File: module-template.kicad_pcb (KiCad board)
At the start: 2 copper layers, 0 parts

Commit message: Added PCB Essentials
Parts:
- added J1: 2X6-HEADERS, EC:M20-7810645, F.Cu at (111.7, 99.5)
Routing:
- net (no net): vias 0 -> 1
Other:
- board outline added: 95 x 25 mm
- board text added: "THIS SIDE DOWN"
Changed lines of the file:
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@@
   )
   (net 0 "")
+  (footprint "EC:M20-7810645" (layer "F.Cu")
+    (at 111.7011 99.5 90)
+    (descr "Harwin M20-7810645 Pass-Through Female Header")
+    (property "Sheetfile" "EC.kicad_sch")
+    (property "Sheetname" "")
+    (fp_text reference "J1" (at 0 0 90) (layer "F.SilkS") hide
+        (effects (font (size 1.27 1.27) (thickness 0.15)))
+    )
+    (fp_text value "2X6-HEADERS" (at 0 0 90) (layer "F.Fab") hide
+        (effects (font (size 1.27 1.27) (thickness 0.15)))
+    )
+    (pad "" np_thru_hole circle (at -6.35 -1.27 90) (size 1.02 1.02) (drill 1.02) (layers "F&B.Cu" "*.Mask"))
+    (pad "" np_thru_hole circle (at -6.35 1.27 90) (size 1.02 1.02) (drill 1.02) (layers "F&B.Cu" "*.Mask"))
+    (pad "" np_thru_hole circle (at -5.08 0 90) (size 1.8 1.8) (drill 1.8) (layers "F&B.Cu" "*.Mask"))
+    (pad "" np_thru_hole circle (at -3.81 -1.27 90) (size 1.02 1.02) (drill 1.02) (layers "F&B.Cu" "*.Mask"))
+    (pad "" np_thru_hole circle (at -3.81 1.27 90) (size 1.02 1.02) (drill 1.02) (layers "F&B.Cu" "*.Mask"))
+    (pad "" np_thru_hole circle (at -1.27 -1.27 90) (size 1.02 1.02) (drill 1.02) (layers "F&B.Cu" "*.Mask"))
+    (pad "" np_thru_hole circle (at -1.27 1.27 90) (size 1.02 1.02) (drill 1.02) (layers "F&B.Cu" "*.Mask"))
+    (pad "" np_thru_hole circle (at 1.27 -1.27 90) (size 1.02 1.02) (drill 1.02) (layers "F&B.Cu" "*.Mask"))
+    (pad "" np_thru_hole circle (at 1.27 1.27 90) (size 1.02 1.02) (drill 1.02) (layers "F&B.Cu" "*.Mask"))
+    (pad "" np_thru_hole circle (at 3.81 -1.27 90) (size 1.02 1.02) (drill 1.02) (layers "F&B.Cu" "*.Mask"))
+    (pad "" np_thru_hole circle (at 3.81 1.27 90) (size 1.02 1.02) (drill 1.02) (layers "F&B.Cu" "*.Mask"))
+    (pad "" np_thru_hole circle (at 5.08 0 90) (size 1.8 1.8) (drill 1.8) (layers "F&B.Cu" "*.Mask"))
+    (pad "" np_thru_hole circle (at 6.35 -1.27 90) (size 1.02 1.02) (drill 1.02) (layers "F&B.Cu" "*.Mask"))
+    (pad "" np_thru_hole circle (at 6.35 1.27 90) (size 1.02 1.02) (drill 1.02) (layers "F&B.Cu" "*.Mask"))
+    (pad "P$1" smd rect (at -6.35 2.91 90) (size 1.02 1.78) (layers "F.Cu" "F.Paste" "F.Mask")
+      (pinfunction "PIN1") (pintype "bidirectional") (solder_mask_margin 0.1016) (thermal_bridge_angle 0))
+    (pad "P$2" smd rect (at -3.81 2.91 90) (size 1.02 1.78) (layers "F.Cu" "F.Paste" "F.Mask")
+      (pinfunction "PIN2") (pintype "bidirectional") (solder_mask_margin 0.1016) (thermal_bridge_angle 0))
+    (pad "P$3" smd rect (at -1.27 2.91 90) (size 1.02 1.78) (layers "F.Cu" "F.Paste" "F.Mask")
+      (pinfunction "PIN3") (pintype "bidirectional") (solder_mask_margin 0.1016) (thermal_bridge_angle 0))
+    (pad "P$4" smd rect (at 1.27 2.91 90) (size 1.02 1.78) (layers "F.Cu" "F.Paste" "F.Mask")
+      (pinfunction "PIN4") (pintype "bidirectional") (solder_mask_margin 0.1016) (thermal_bridge_angle 0))
+    (pad "P$5" smd rect (at 3.81 2.91 90) (size 1.02 1.78) (layers "F.Cu" "F.Paste" "F.Mask")
+      (pinfunction "PIN5") (pintype "bidirectional") (solder_mask_margin 0.1016) (thermal_bridge_angle 0))
+    (pad "P$6" smd rect (at 6.35 2.91 90) (size 1.02 1.78) (layers "F.Cu" "F.Paste" "F.Mask")
+      (pinfunction "PIN6") (pintype "bidirectional") (solder_mask_margin 0.1016) (thermal_bridge_angle 0))
+    (pad "P$7" smd rect (at 6.35 -2.91 90) (size 1.02 1.78) (layers "F.Cu" "F.Paste" "F.Mask")
+      (pinfunction "PIN7") (pintype "bidirectional") (solder_mask_margin 0.1016) (thermal_bridge_angle 0))
+    (pad "P$8" smd rect (at 3.81 -2.91 90) (size 1.02 1.78) (layers "F.Cu" "F.Paste" "F.Mask")
+      (pinfunction "PIN8") (pintype "bidirectional") (solder_mask_margin 0.1016) (thermal_bridge_angle 0))
+    (pad "P$9" smd rect (at 1.27 -2.91 90) (size 1.02 1.78) (layers "F.Cu" "F.Paste" "F.Mask")
+      (pinfunction "PIN9") (pintype "bidirectional") (solder_mask_margin 0.1016) (thermal_bridge_angle 0))
+    (pad "P$10" smd rect (at -1.27 -2.91 90) (size 1.02 1.78) (layers "F.Cu" "F.Paste" "F.Mask")
+      (pinfunction "PIN10") (pintype "bidirectional") (solder_mask_margin 0.1016) (thermal_bridge_angle 0))
+    (pad "P$11" smd rect (at -3.81 -2.91 90) (size 1.02 1.78) (layers "F.Cu" "F.Paste" "F.Mask")
+      (pinfunction "PIN11") (pintype "bidirectional") (solder_mask_margin 0.1016) (thermal_bridge_angle 0))
+    (pad "P$12" smd rect (at -6.35 -2.91 90) (size 1.02 1.78) (layers "F.Cu" "F.Paste" "F.Mask")
+      (pinfunction "PIN12") (pintype "bidirectional") (solder_mask_margin 0.1016) (thermal_bridge_angle 0))
+  )
+  (gr_circle (center 99.2 99.5) (end 103.2 99.5)
+    (stroke (width 0) (type solid)) (fill solid) (layer "F.Cu"))
+  (gr_arc (start 104.2011 90) (mid 103.32242 92.12132) (end 101.2011 93)
+    (stroke (width 0.05) (type solid)) (layer "Edge.Cuts"))
+  (gr_line (start 186.2011 87) (end 107.2011 87)
+    (stroke (width 0.05) (type solid)) (layer "Edge.Cuts"))
+  (gr_line (start 107.2011 112) (end 186.2011 112)
+    (stroke (width 0.05) (type solid)) (layer "Edge.Cuts"))
+  (gr_arc (start 104.2011 90) (mid 105.07978 87.87868) (end 107.2011 87)
+    (stroke (width 0.05) (type solid)) (layer "Edge.Cuts"))
+  (gr_line (start 97.2011 106) (end 101.2011 106)
+    (stroke (width 0.05) (type solid)) (layer "Edge.Cuts"))
+  (gr_arc (start 94.2011 96) (mid 95.07978 93.87868) (end 97.2011 93)
+    (stroke (width 0.05) (type solid)) (layer "Edge.Cuts"))
+  (gr_line (start 94.2011 96) (end 94.2011 103)
+    (stroke (width 0.05) (type solid)) (layer "Edge.Cuts"))
+  (gr_line (start 189.2011 109) (end 189.2011 90)
+    (stroke (width 0.05) (type solid)) (layer "Edge.Cuts"))
+  (gr_arc (start 189.2011 109) (mid 188.32242 111.12132) (end 186.2011 112)
+    (stroke (width 0.05) (type solid)) (layer "Edge.Cuts"))
+  (gr_arc (start 97.2011 106) (mid 95.07978 105.12132) (end 94.2011 103)
+    (stroke (width 0.05) (type solid)) (layer "Edge.Cuts"))
+  (gr_arc (start 107.2011 112) (mid 105.07978 111.12132) (end 104.2011 109)
+    (stroke (width 0.05) (type solid)) (layer "Edge.Cuts"))
+  (gr_line (start 101.2011 93) (end 97.2011 93)
+    (stroke (width 0.05) (type solid)) (layer "Edge.Cuts"))
+  (gr_arc (start 101.2011 106) (mid 103.32242 106.87868) (end 104.2011 109)
+    (stroke (width 0.05) (type solid)) (layer "Edge.Cuts"))
+  (gr_arc (start 186.2011 87) (mid 188.32242 87.87868) (end 189.2011 90)
+    (stroke (width 0.05) (type solid)) (layer "Edge.Cuts"))
+  (gr_text "THIS\nSIDE\nDOWN" (at 173.7011 99.5) (layer "B.SilkS")
+    (effects (font (size 2.61 2.61) (thickness 0.39)) (justify mirror))
+  )
+  (via (at 162.7011 99.5) (size 6) (drill 3.6) (layers "F.Cu" "B.Cu") (net 0))
+  (zone (net 0) (net_name "") (layers "*.Mask") (hatch edge 0.5)
+    (connect_pads (clearance 0.25))
+    (min_thickness 0.25) (filled_areas_thickness no)
+    (fill yes (thermal_gap 0.5) (thermal_bridge_width 0.5))
+    (polygon
+      (pts
+        (xy 104.2 88.4964)
+        (xy 104.2 110.4964)
+        (xy 93.2 110.4964)
+        (xy 93.2 88.4964)
+      )
+    )
+  )
 )

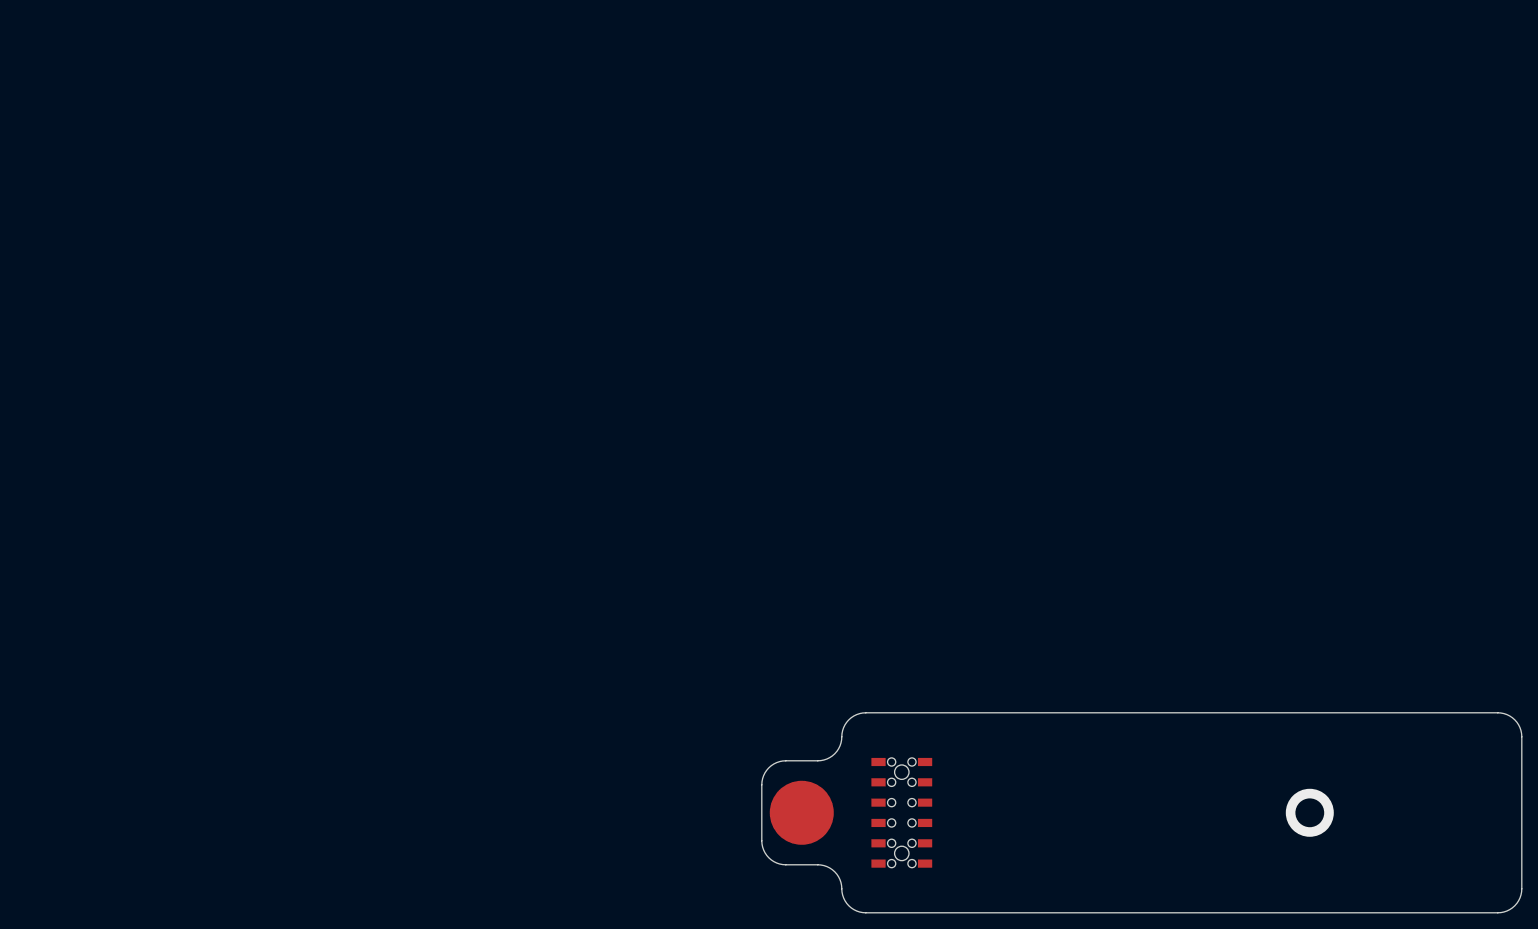
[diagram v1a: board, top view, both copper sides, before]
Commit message: PCB Notes, Sheet size adjustment.
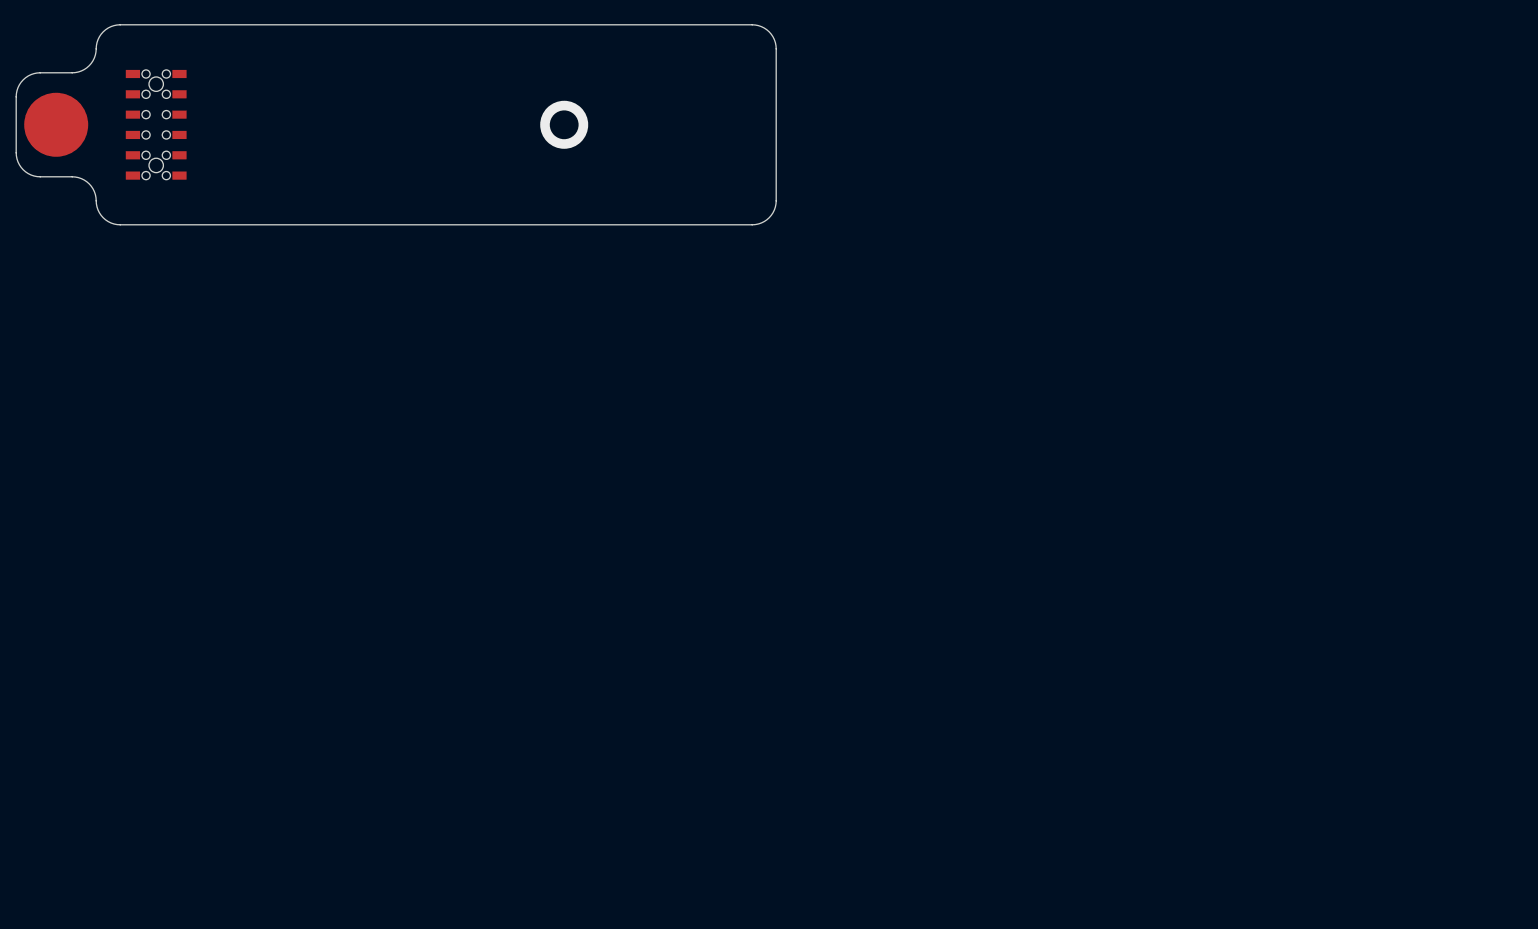
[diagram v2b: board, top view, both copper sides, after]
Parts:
- moved J1 126.8 mm to (18.5, 13.5)
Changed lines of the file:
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@@
     (thickness 1.6)
   )
-  (paper "USLetter")
+  (paper "User" 97.0026 27.0002)
   (layers
     (0 "F.Cu" signal)
@@
   (net 0 "")
   (footprint "EC:M20-7810645" (layer "F.Cu")
-    (at 111.7011 99.5 90)
+    (at 18.5 13.5 90)
     (descr "Harwin M20-7810645 Pass-Through Female Header")
     (property "Sheetfile" "EC.kicad_sch")
@@
       (pinfunction "PIN12") (pintype "bidirectional") (solder_mask_margin 0.1016) (thermal_bridge_angle 0))
   )
-  (gr_circle (center 99.2 99.5) (end 103.2 99.5)
+  (gr_circle (center 6 13.5) (end 10 13.5)
     (stroke (width 0) (type solid)) (fill solid) (layer "F.Cu"))
-  (gr_arc (start 104.2011 90) (mid 103.32242 92.12132) (end 101.2011 93)
+  (gr_line (start 4 10) (end 2 10)
+    (stroke (width 0.15) (type default)) (layer "Dwgs.User"))
+  (gr_line (start 67 10) (end 52 -7)
+    (stroke (width 0.4) (type default)) (layer "Dwgs.User"))
+  (gr_line (start 67 10) (end 65 10)
+    (stroke (width 0.15) (type default)) (layer "Dwgs.User"))
+  (gr_line (start 67 8) (end 67 10)
+    (stroke (width 0.4) (type default)) (layer "Dwgs.User"))
+  (gr_line (start 65 10) (end 67 10)
+    (stroke (width 0.4) (type default)) (layer "Dwgs.User"))
+  (gr_line (start 4 10) (end -11 -7)
+    (stroke (width 0.4) (type default)) (layer "Dwgs.User"))
+  (gr_line (start 4 8) (end 4 10)
+    (stroke (width 0.4) (type default)) (layer "Dwgs.User"))
+  (gr_line (start 2 10) (end 4 10)
+    (stroke (width 0.4) (type default)) (layer "Dwgs.User"))
+  (gr_arc (start 11 4) (mid 10.12132 6.12132) (end 8 7)
     (stroke (width 0.05) (type solid)) (layer "Edge.Cuts"))
-  (gr_line (start 186.2011 87) (end 107.2011 87)
+  (gr_line (start 93 1) (end 14 1)
     (stroke (width 0.05) (type solid)) (layer "Edge.Cuts"))
-  (gr_line (start 107.2011 112) (end 186.2011 112)
+  (gr_line (start 14 26) (end 93 26)
     (stroke (width 0.05) (type solid)) (layer "Edge.Cuts"))
-  (gr_arc (start 104.2011 90) (mid 105.07978 87.87868) (end 107.2011 87)
+  (gr_arc (start 11 4) (mid 11.87868 1.87868) (end 14 1)
     (stroke (width 0.05) (type solid)) (layer "Edge.Cuts"))
-  (gr_line (start 97.2011 106) (end 101.2011 106)
+  (gr_line (start 4 20) (end 8 20)
     (stroke (width 0.05) (type solid)) (layer "Edge.Cuts"))
-  (gr_arc (start 94.2011 96) (mid 95.07978 93.87868) (end 97.2011 93)
+  (gr_arc (start 1 10) (mid 1.87868 7.87868) (end 4 7)
     (stroke (width 0.05) (type solid)) (layer "Edge.Cuts"))
-  (gr_line (start 94.2011 96) (end 94.2011 103)
+  (gr_line (start 1 10) (end 1 17)
     (stroke (width 0.05) (type solid)) (layer "Edge.Cuts"))
-  (gr_line (start 189.2011 109) (end 189.2011 90)
+  (gr_line (start 96 23) (end 96 4)
     (stroke (width 0.05) (type solid)) (layer "Edge.Cuts"))
-  (gr_arc (start 189.2011 109) (mid 188.32242 111.12132) (end 186.2011 112)
+  (gr_arc (start 96 23) (mid 95.12132 25.12132) (end 93 26)
     (stroke (width 0.05) (type solid)) (layer "Edge.Cuts"))
-  (gr_arc (start 97.2011 106) (mid 95.07978 105.12132) (end 94.2011 103)
+  (gr_arc (start 4 20) (mid 1.87868 19.12132) (end 1 17)
     (stroke (width 0.05) (type solid)) (layer "Edge.Cuts"))
-  (gr_arc (start 107.2011 112) (mid 105.07978 111.12132) (end 104.2011 109)
+  (gr_arc (start 14 26) (mid 11.87868 25.12132) (end 11 23)
     (stroke (width 0.05) (type solid)) (layer "Edge.Cuts"))
-  (gr_line (start 101.2011 93) (end 97.2011 93)
+  (gr_line (start 8 7) (end 4 7)
     (stroke (width 0.05) (type solid)) (layer "Edge.Cuts"))
-  (gr_arc (start 101.2011 106) (mid 103.32242 106.87868) (end 104.2011 109)
+  (gr_arc (start 8 20) (mid 10.12132 20.87868) (end 11 23)
     (stroke (width 0.05) (type solid)) (layer "Edge.Cuts"))
-  (gr_arc (start 186.2011 87) (mid 188.32242 87.87868) (end 189.2011 90)
+  (gr_arc (start 93 1) (mid 95.12132 1.87868) (end 96 4)
     (stroke (width 0.05) (type solid)) (layer "Edge.Cuts"))
-  (gr_text "THIS\nSIDE\nDOWN" (at 173.7011 99.5) (layer "B.SilkS")
-    (effects (font (size 2.61 2.61) (thickness 0.39)) (justify mirror))
+  (gr_text "THIS\nSIDE\nDOWN" (at 84.7989 13.5) (layer "B.SilkS")
+    (effects (font (size 2.61 2.61) (thickness 0.522) bold) (justify mirror))
   )
-  (via (at 162.7011 99.5) (size 6) (drill 3.6) (layers "F.Cu" "B.Cu") (net 0))
+  (gr_text_box "This is a hard mounting point\nfor FieldKit Modules.\nYou shouldn't connect it to any net.\nYou definitely shouldn't delete it.\nSeriously, don't delete it."
+    (start 27 -17) (end 59 -7) (layer "Dwgs.User")
+      (effects (font (size 1 1) (thickness 0.15)) (justify top))
+    (stroke (width 0.4) (type solid))  )
+  (gr_text_box "By convention, Icons for modules are :\n- Round\n- 8mm in Diameter\n- on F.Cu\n- Centered at 6 x 13.5"
+    (start -11 -17) (end 23 -7) (layer "Dwgs.User")
+      (effects (font (size 1 1) (thickness 0.15)) (justify top))
+    (stroke (width 0.4) (type solid))  )
+  (via (at 69.5 13.5) (size 6) (drill 3.6) (layers "F.Cu" "B.Cu") (net 0))
   (zone (net 0) (net_name "") (layers "*.Mask") (hatch edge 0.5)
     (connect_pads (clearance 0.25))
@@
     (polygon
       (pts
-        (xy 104.2 88.4964)
-        (xy 104.2 110.4964)
-        (xy 93.2 110.4964)
-        (xy 93.2 88.4964)
+        (xy 10.9989 2.4964)
+        (xy 10.9989 24.4964)
+        (xy -0.0011 24.4964)
+        (xy -0.0011 2.4964)
       )
     )

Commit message: Finished prerequisites. Started component placement.
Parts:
- added C1: 1µf, !magpie:R0603, F.Cu at (28.5, 7.50)
- added C2: 1µf, !magpie:R0603, F.Cu at (28.5, 9.80)
- added C3: .1μf, !magpie:R0603, F.Cu at (28.2, 19.7)
- added R1: 10kΩ, !magpie:R0603, F.Cu at (24.9, 5.80)
- added R2: 4.7kΩ, !magpie:R0603, F.Cu at (25.7, 19.7)
- added R3: 4.7kΩ, !magpie:R0603, F.Cu at (24.4, 19.7)
- added U1: AP2127K-3.3, Package_TO_SOT_SMD:SOT-23-5, F.Cu at (25.4, 8.62)
- added U2: M24C64-DFMN6TP, Package_SO:SOIC-8_3.9x4.9mm_P1.27mm, F.Cu at (26.3, 14.6)

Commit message: Board routing complete.
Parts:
- J1: value 2X6-HEADERS -> Conn_01x12; footprint EC:M20-7810645 -> !magpie:M20-7810645R
- moved C2 1.00 mm to (27.9, 9.00), turned to 90 degrees
- moved C1 0.91 mm to (28.4, 6.60)
- moved R1 0.74 mm to (24.4, 5.25), turned to 90 degrees
- turned J1 to -90 degrees
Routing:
- net /Module-Prerequisites/HOST-3V3: track 0.00 -> 22.5 mm
- net /Module-Prerequisites/VIN: track 0.00 -> 20.5 mm, vias 0 -> 2
- net /Module-Prerequisites/ENABLE: track 0.00 -> 16.8 mm
- net /Module-Prerequisites/3V3: track 0.00 -> 14.9 mm, vias 0 -> 2
- net /Module-Prerequisites/SDA: track 0.00 -> 9.11 mm, vias 0 -> 2
- net /Module-Prerequisites/SCL: track 0.00 -> 7.98 mm
- net GND: vias 0 -> 3
- added copper zone on B.Cu, net GND
- added copper zone on F.Cu, net GND
